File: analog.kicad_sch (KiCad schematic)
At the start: 12 parts, among them U2 ADS124S08

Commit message: progressing, blocking things out, pondering orbz
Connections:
- net INA+: now also U2.3 (AIN4); no longer U2.5 (AIN2)
- net INA-: now also U2.2 (AIN5); no longer U2.4 (AIN3)
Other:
- note added: "But at least, one more diff pair? And pin headers for them?"
- note added: "VDDA and... what? are my excitation choices? Offer solder jumpers for the IDAC?"
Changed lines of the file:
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@@
+		)
+	)
+	(text "VDDA and... what? are my excitation choices?\nOffer solder jumpers for the IDAC?"
+		(exclude_from_sim no)
+		(at 59.182 163.576 0)
+		(effects
+			(font
+				(size 1.27 1.27)
+			)
 		)
 	)
@@
 		)
 	)
+	(text "But at least, one more diff pair?\nAnd pin headers for them?"
+		(exclude_from_sim no)
+		(at 179.832 160.02 0)
+		(effects
+			(font
+				(size 1.27 1.27)
+			)
+		)
+	)
 	(text "vdda is 5v\n"
 		(exclude_from_sim no)
@@
 	(wire
 		(pts
-			(xy 127 93.98) (xy 142.24 93.98)
+			(xy 127 99.06) (xy 142.24 99.06)
 		)
 		(stroke
@@
 	(wire
 		(pts
-			(xy 127 91.44) (xy 142.24 91.44)
+			(xy 127 96.52) (xy 142.24 96.52)
 		)
 		(stroke
@@
 	)
 	(label "INA-"
-		(at 127 93.98 0)
+		(at 127 99.06 0)
 		(effects
 			(font
@@
 	)
 	(label "INA+"
-		(at 127 91.44 0)
-		(effects
-			(font
+		(at 127 96.52 0)
+		(effects
+			(font

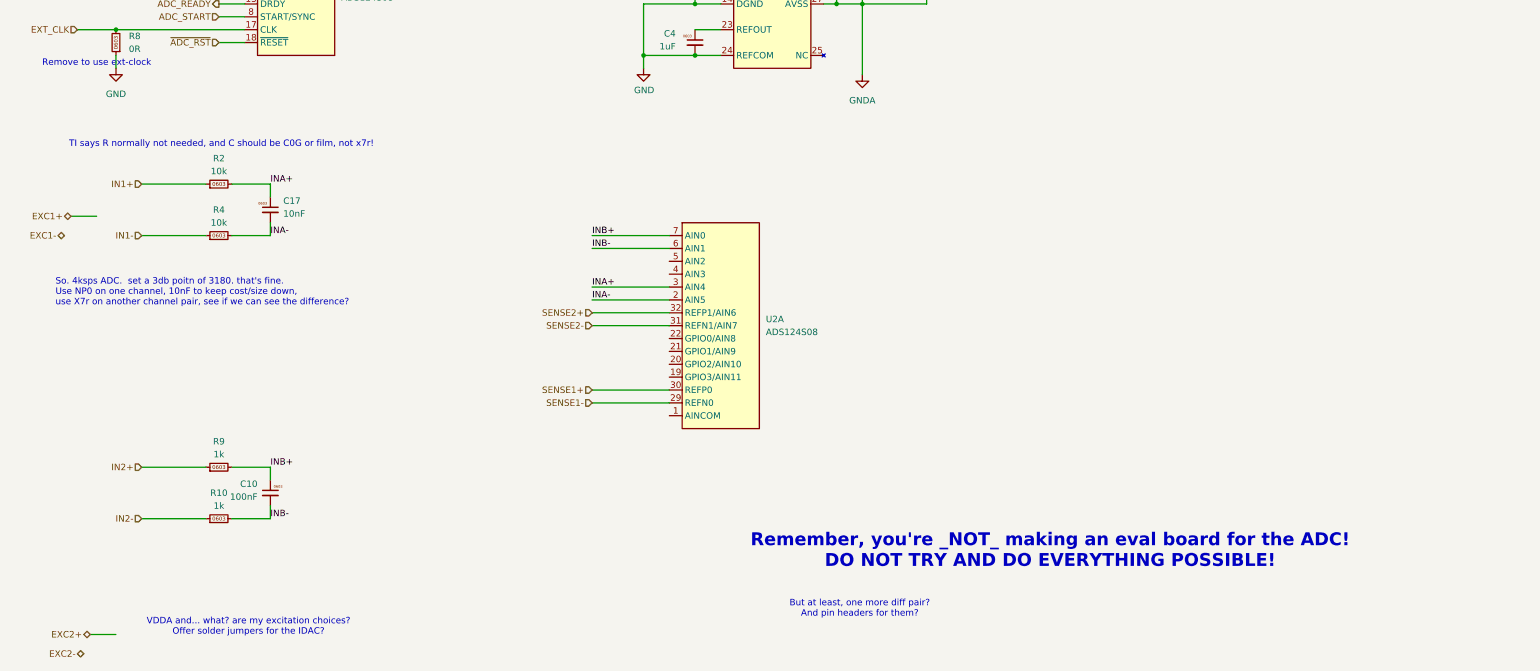
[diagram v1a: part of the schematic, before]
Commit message: notes and tweaks.
notes on inputs, filter ref, spi series R.
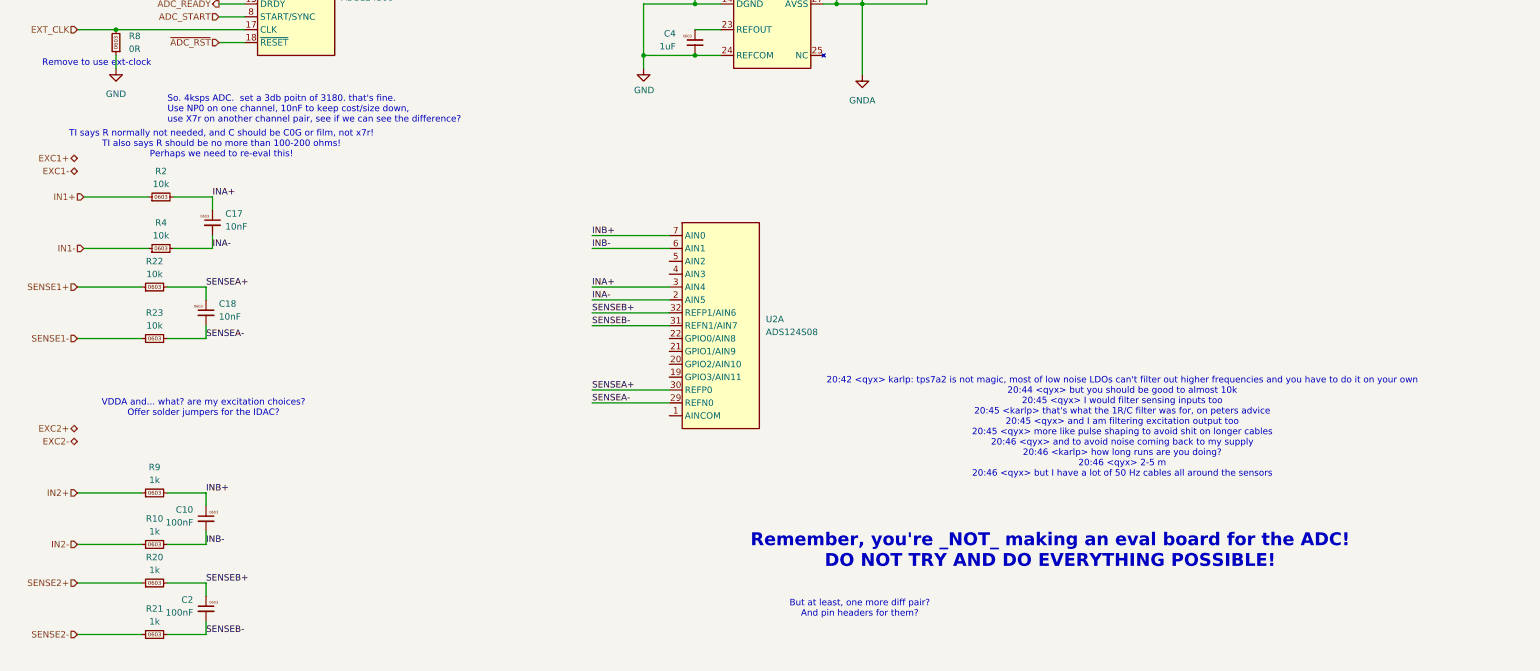
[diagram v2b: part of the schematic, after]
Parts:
- added C18: 10nF, Capacitor_SMD:C_0603_1608Metric, symbol karl-marel-atomics:KC0603_10nF_C0G
- added C2: 100nF, Capacitor_SMD:C_0603_1608Metric, symbol karl-marel-atomics:KC0603_100nF
- added R20, R21: 1k, Resistor_SMD:R_0603_1608Metric, symbol karl-marel-atomics:KR0603_1k
- added R22, R23: 10k, Resistor_SMD:R_0603_1608Metric, symbol karl-marel-atomics:KR0603_10k
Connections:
- net SENSE1+: now also R22.1; no longer U2.30 (REFP0)
- net SENSE1-: now also R23.1; no longer U2.29 (REFN0)
- net SENSE2+: now also R20.1; no longer U2.32 (REFP1/AIN6)
- net SENSE2-: now also R21.1; no longer U2.31 (REFN1/AIN7)
- new net SENSEA+: C18.1, R22.2, U2.30 (REFP0)
- new net SENSEA-: C18.2, R23.2, U2.29 (REFN0)
- new net SENSEB+: C2.1, R20.2, U2.32 (REFP1/AIN6)
- new net SENSEB-: C2.2, R21.2, U2.31 (REFN1/AIN7)
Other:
- note added: "20:42 <qyx> karlp: tps7a2 is not magic, most of low noise LDOs can't filter out higher frequencies and you have to do it on your own 20:44 <qyx> but you should be good to almost 10k 20:45 <qyx> I would filter sensing inputs too 20:45 <karlp> that's what the 1R/C filter was for, on peters advice 20:45 <qyx> and I am filtering excitation output too 20:45 <qyx> more like pulse shaping to avoid shit 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"
- note added: "TI says R normally not needed, and C should be C0G or film, not x7r! TI also says R should be no more than 100-200 ohms! Perhaps we need to re-eval this!"
- note removed: "TI says R normally not needed, and C should be C0G or film, not x7r!"
- moved on the sheet: C10, C17, R10, R2, R4, R9

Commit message: overhausl inputs a lot
read too much, thought too much.
try one with the "just 0R plus a nice big good quality cap" from the TI
precision seminar, describing common realities, as well as mixing in
what they did on the ads1262ref scale design document for the second
channel with a more "full blown" input filter.

I don't really like how none of this seems to be a proper AA filter,
but... ok.
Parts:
- removed C10, C2: 100nF, Capacitor_SMD:C_0603_1608Metric, symbol karl-marel-atomics:KC0603_100nF
- removed C17, C18: 10nF, Capacitor_SMD:C_0603_1608Metric, symbol karl-marel-atomics:KC0603_10nF_C0G
- removed R10, R20, R21, R9: 1k, Resistor_SMD:R_0603_1608Metric, symbol karl-marel-atomics:KR0603_1k
- removed R2, R22, R23, R4: 10k, Resistor_SMD:R_0603_1608Metric, symbol karl-marel-atomics:KR0603_10k
- added C10, C17, C18, C2: 220nF, Capacitor_SMD:C_1206_3216Metric, symbol karl-atomic-basic:KC1206_220nF_C0G
- added C19, C24, C25, C26: 100pF, Capacitor_SMD:C_0603_1608Metric, symbol karl-atomic-basic:KC0603_100pF
- added C20, C21, C22, C23: 1uF, symbol Device:C_Feedthrough
- added C27, C28: 1uF, Capacitor_SMD:C_0603_1608Metric, symbol karl-atomic-basic:KC0603_1uF
- added R2, R22, R23, R4: 0R, Resistor_SMD:R_0603_1608Metric, symbol karl-atomic-basic:KR0603_0R
- added RN1: 47R, Resistor_SMD:R_Array_Convex_4x0603, symbol Device:R_Pack04
- C3: symbol karl-marel-atomics:KC0603_100nF -> karl-atomic-basic:KC0603_100nF
- C4: symbol karl-marel-atomics:KC0603_1uF -> karl-atomic-basic:KC0603_1uF
- C5, C9: symbol karl-marel-atomics:KC0603_220nF -> karl-atomic-basic:KC0603_220nF; jlcbasic (none) -> basic
- R8: symbol karl-marel-atomics:KR0603_0R -> karl-atomic-basic:KR0603_0R
- U2: symbol karl-marel-atomics:ADS124S08IPBSR -> karl-atomic-basic:ADS124S08IPBSR
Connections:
- net EXC1+: now also C27.1
- net EXC2+: now also C28.1
- net GNDA: now also C19.2, C20.2, C21.2, C22.2, C23.2, C24.2, C25.2, C26.2, C27.2, C28.2
- net IN1+: now also R2.1
- net IN1-: now also R4.1
- net IN2+: now also RN1.1 (R1.1)
- net IN2-: now also RN1.2 (R2.1)
- net INA+: now also C17.1, R2.2
- net INA-: now also C17.2, R4.2
- net INB+: now also C10.1, C20.3, C26.1
- net INB-: now also C10.2, C21.1, C25.1
- net SENSE1+: now also R22.1
- net SENSE1-: now also R23.1
- net SENSE2+: now also RN1.3 (R3.1)
- net SENSE2-: now also RN1.4 (R4.1)
- net SENSEA+: now also C18.1, R22.2
- net SENSEA-: now also C18.2, R23.2
- net SENSEB+: now also C2.1, C22.3, C24.1
- net SENSEB-: now also C19.1, C2.2, C23.1
- new net: C23.3, RN1.5 (R4.2)
- new net: C22.1, RN1.6 (R3.2)
- new net: C21.3, RN1.7 (R2.2)
- new net: C20.1, RN1.8 (R1.2)
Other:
- note added: "100nF C0g zero R for this channel"
- note added: "Is an array _realllly_ better matched?"
- note added: "Ok Channel A: TI seminar: 0R + small diff cap only, C0G. Channel B: LowR+diffcap+CM caps? C0G?"
- note added: "Place one, size, order with LCSC for alts to try out? 0805 is best for getting a viable voltage...? note these are _10c_ caps! the money1!!1!!!! NFM21PC105B1C3D 16V, 1uF, 0805 < cheap, pretty good choice? YFF21PC1C474MT000N 16V 470nF, 0805 NFM21PC104R1E3D 25V 100nF 0805 NFM21CC223R1H3D 50V 22nF, 0805 NFM18HC105C1C3D 16V, 1uF, 0603 size NFM18PC104R1C3D 16V 100nF, 0603 NFM18CC223R1C3D 16V 22nF, 0603"
- note added: "TODO: filter excitations each? TODO: pins for spare ads/gpios/idac?"
- note added: "Then this cahnnel, 47R array, 100nF feeds?"
- note added: "so.. ads124s08 has ext ref input impedance of 250kR ads1262 has ext ref input impedance of 50_MR_ But... we're getting the ref back from sense lines with like 350ohms? so... no big deal?"
- moved on the sheet: U2A

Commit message: thanks, I hate it.
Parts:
- C20, C21, C22, C23: footprint (none) -> jlc-extras:C_Feedthrough_NFM21_2.0mmx1.2mm
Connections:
- net IN2+: now also RN1.3 (R3.1); no longer RN1.1 (R1.1)
- net SENSE2+: now also RN1.4 (R4.1); no longer RN1.3 (R3.1)
- net SENSE2-: now also RN1.1 (R1.1); no longer RN1.4 (R4.1)
- net at C23.3: now also RN1.8 (R1.2); no longer RN1.5 (R4.2)
- net at C22.1: now also RN1.5 (R4.2); no longer RN1.6 (R3.2)
- net at C20.1: now also RN1.6 (R3.2); no longer RN1.8 (R1.2)
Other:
- note added: "So, this is RC of 47+1uF+220nF/2? fcutoff of then 6kHz? I think I should reduce the feed caps? YES! this was frrom an ADS12_3_2 design, which is only 80SPS!"
- note added: "actual ads124s08 evm uses 4.12k+4.7nF diff caps"
- moved on the sheet: RN1

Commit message: moarh updates
we commit to save our progress
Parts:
- added C29: 10nF, Capacitor_SMD:C_0603_1608Metric, symbol karl-atomic-basic:KC0603_10nF
- added D4: LED_0805_Yellow, LED_SMD:LED_0805_2012Metric, symbol karl-atomic-basic:LED_0805_Yellow
- added D5: LED_0805_Red, LED_SMD:LED_0805_2012Metric, symbol karl-atomic-basic:LED_0805_Red
- added D6: LED_0805_Green, LED_SMD:LED_0805_2012Metric, symbol karl-atomic-basic:LED_0805_Green
- added J10, J11: Conn_01x02, Connector_Phoenix_MC:PhoenixContact_MCV_1,5_2-G-3.81_1x02_P3.81mm_Vertical, symbol Connector_Generic:Conn_01x02
- added J9: Conn_01x03, Connector_PinHeader_2.54mm:PinHeader_1x03_P2.54mm_Vertical, symbol Connector_Generic:Conn_01x03
- added R10, R20, R9: 1k, Resistor_SMD:R_0603_1608Metric, symbol karl-atomic-basic:KR0603_1k
- added R21, R24: 5k1, Resistor_SMD:R_0603_1608Metric, symbol karl-atomic-basic:KR0603_5k1
- added R25: 0R, Resistor_SMD:R_0603_1608Metric, symbol karl-atomic-basic:KR0603_0R
- U2: footprint Package_QFP:TQFP-32_5x5mm_P0.5mm -> Package_QFP:LQFP-32_5x5mm_P0.5mm
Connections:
- net EXC2+ is gone; now on net EXC1+: C28.1
- net +3V3: now also D4.1 (K), D5.1 (K), D6.1 (K)
- net EXC1+: now also J11.1 (Pin_1), R25.1
- net IN2+: now also RN1.4 (R4.1); no longer RN1.3 (R3.1)
- net IN2-: now also RN1.3 (R3.1); no longer RN1.2 (R2.1)
- net INB+: now also U2.5 (AIN2); no longer U2.7 (AIN0)
- net INB-: now also U2.4 (AIN3); no longer U2.6 (AIN1)
- net SENSE2+: now also RN1.2 (R2.1); no longer RN1.4 (R4.1)
- net VDDA: now also R25.2
- net AINCOM: now reaches U2.1 (AINCOM)
- net AINCOM: now also J11.2 (Pin_2)
- net at U2.19 (GPIO3/AIN11): now also J9.1 (Pin_1), R10.2
- net at U2.20 (GPIO2/AIN10): now also J9.2 (Pin_2), R9.2
- net at U2.21 (GPIO1/AIN9): now also J9.3 (Pin_3), R20.2
- net at RN1.5 (R4.2): now also C20.1; no longer C22.1
- net at RN1.6 (R3.2): now also C21.3; no longer C20.1
- net at RN1.7 (R2.2): now also C22.1; no longer C21.3
- new net: D4.2 (A), R20.1
- new net: D5.2 (A), R9.1
- new net: D6.2 (A), R10.1
- new net IN3+: J10.2 (Pin_2), R21.1
- new net IN3-: J10.1 (Pin_1), R24.1
- new net INC+: C29.1, R21.2, U2.7 (AIN0)
- new net INC-: C29.2, R24.2, U2.6 (AIN1)
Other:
- note added: "Bonus: "unthinking" basic 6kHz AA filter"
- note added: "So, this is RC of 47+1uF+220nF/2? fcutoff of then 6kHz? I think I should reduce the feed caps? YES! this was frrom an ADS12_3_2 design, which is only 80SPS! FIXME: you still need to reduce these caps! at least the feedtrhough!"
- note added: "VDDA and... what? are my excitation choices? Offer solder jumpers for the IDAC? No, screw the idacs. Allow fiddling with VExcite instead"
- note added: "can try one more _input_ filter, but have to use existing ref filters? just on pins? Try a basic, x7r, "no thinking" see how bad it is?"
- note removed: "So, this is RC of 47+1uF+220nF/2? fcutoff of then 6kHz? I think I should reduce the feed caps? YES! this was frrom an ADS12_3_2 design, which is only 80SPS!"
- note removed: "VDDA and... what? are my excitation choices? Offer solder jumpers for the IDAC?"
- moved on the sheet: U2A

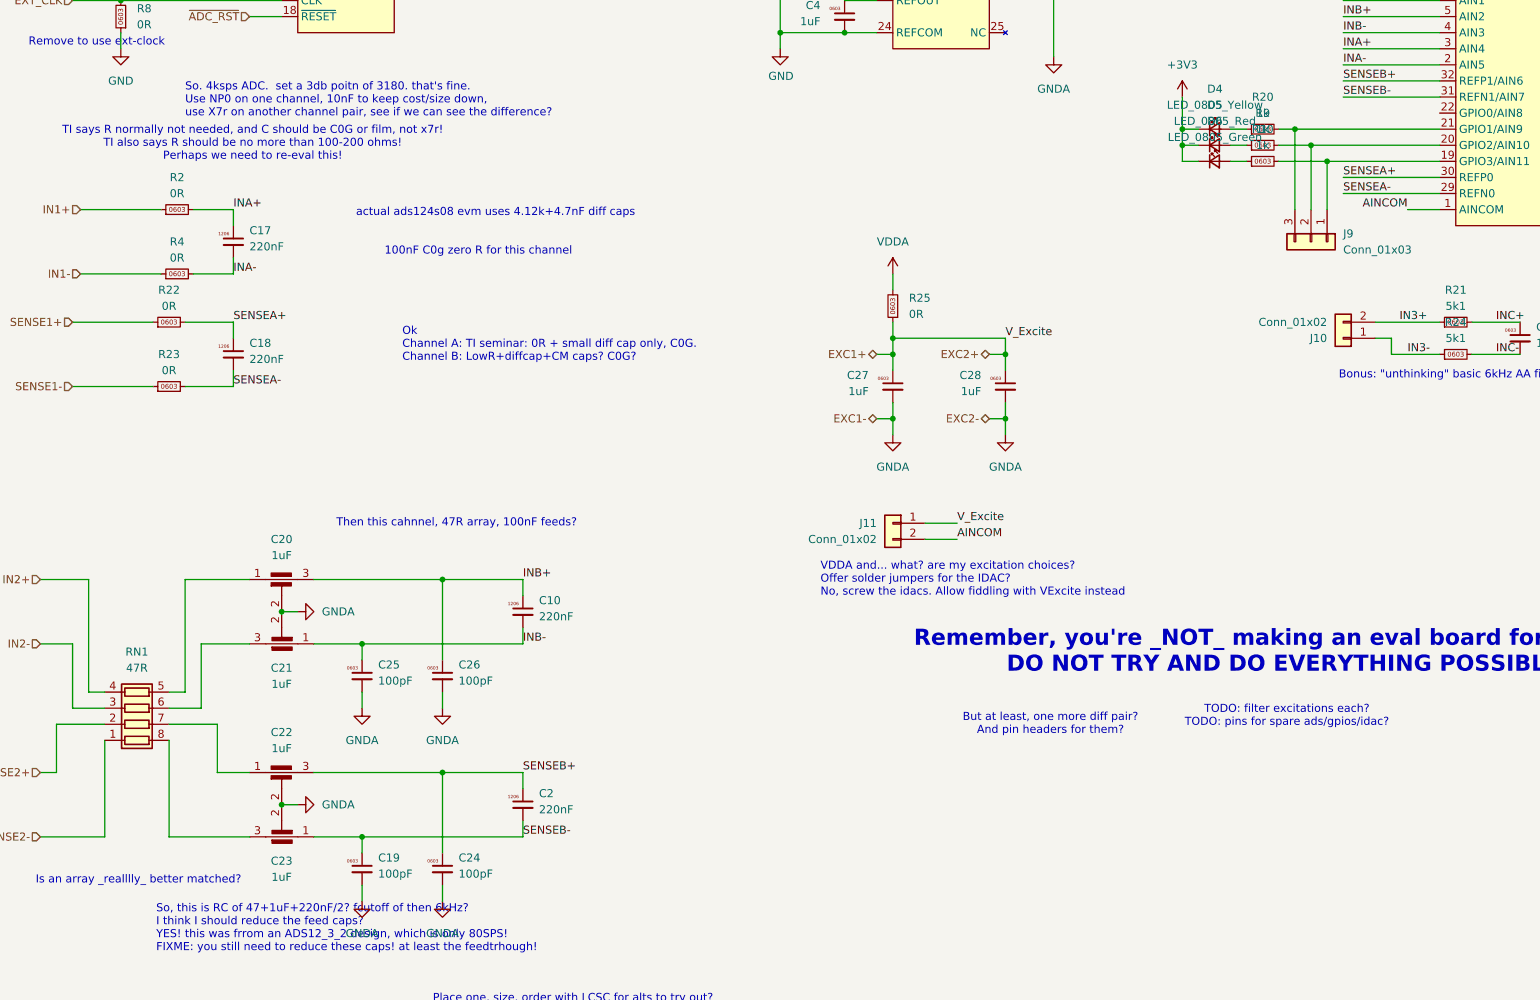
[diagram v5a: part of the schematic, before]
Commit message: "ready" ?
Added 0805 footprints for the diff caps, to try different values there.
for the smaller nF values, 080 is _way_ cheaper than the 1206 that's
~required for the big nF values.

Pushed a lot of silk....
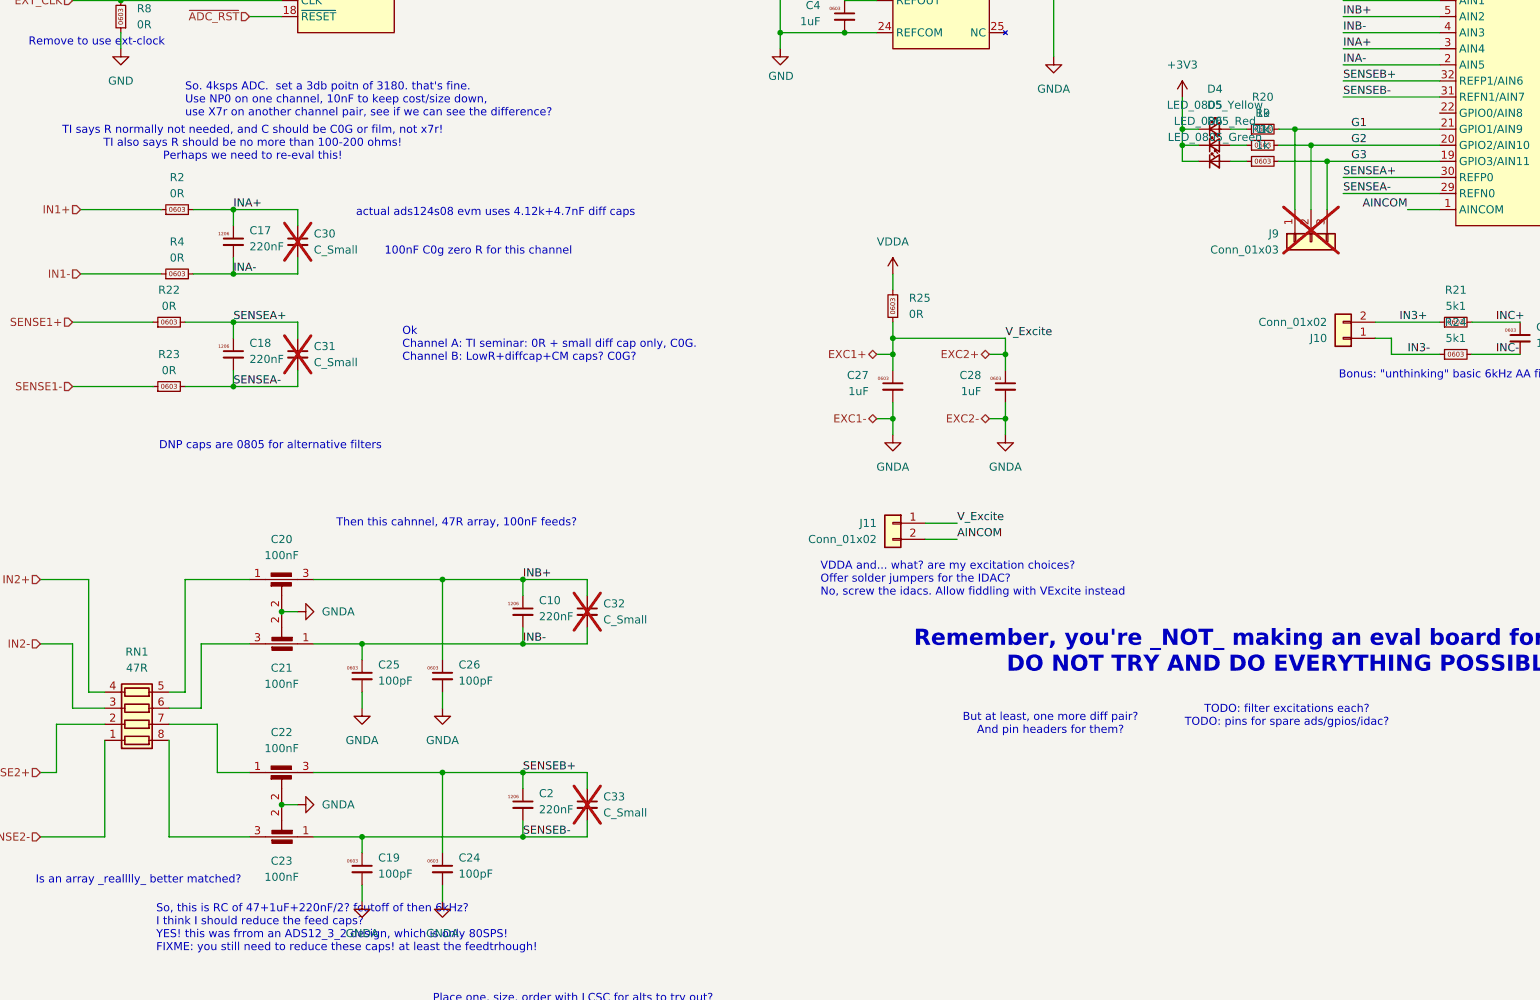
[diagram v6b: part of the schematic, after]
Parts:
- added C30, C31, C32, C33: C_Small, Capacitor_SMD:C_0805_2012Metric, symbol Device:C_Small
- C20, C21, C22, C23: value 1uF -> 100nF; LCSC Part # C92518 -> C86150; MPN NFM21PC105B1C3D -> NFM21PC104R1E3D
- J9: now not fitted
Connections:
- net INA+: now also C30.1
- net INA-: now also C30.2
- net INB+: now also C32.1
- net INB-: now also C32.2
- net SENSEA+: now also C31.1
- net SENSEA-: now also C31.2
- net SENSEB+: now also C33.1
- net SENSEB-: now also C33.2
- net G1: now reaches R20.2, U2.21 (GPIO1/AIN9)
- net G1: now also J9.1 (Pin_1); no longer J9.3 (Pin_3)
- net G3: now reaches R10.2, U2.19 (GPIO3/AIN11)
- net G3: now also J9.3 (Pin_3); no longer J9.1 (Pin_1)
- net G2: now reaches J9.2 (Pin_2), R9.2, U2.20 (GPIO2/AIN10)
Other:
- note added: "DNP caps are 0805 for alternative filters"
